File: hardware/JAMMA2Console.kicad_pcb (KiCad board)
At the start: 4 copper layers, 126 x 131.5 mm, 195 parts, among them J1 Conn_02x28_JAMMA, J10 Conn_02x03_Odd_Even, J11 Conn_02x05_Odd_Even, J12 Conn_01x03, J13 Conn_01x03, J2 DS1038-15FBNSiA74-0CC, J3 SCART-F, J4 DF1BZ-34DP-2.5DSA, J5 PJ-320D, J6 DS1037-15FNAKT74-0CC, J7 DS1037-15FNAKT74-0CC, J8 Phoenix PTS 1,5/4-5.0, J9 Molex 67503-1020, SW1 SW_Push, SW2 SW_Push, SW3 SW_Push, U1 USBLC6-2P6, U10 74LVC4245, U11 74LVC4245, U12 TL074, U13 LM1972, U14 TPA3138D2, U15 74HCT4053, U2 LD1117-3.3, U3 74HCT4053, U4 74HCT86, U5 74HCT4053, U6 LM1881, U7 THS7375, U8 STM32F103V8Tx, U9 74LVC4245, Y1 12MHz

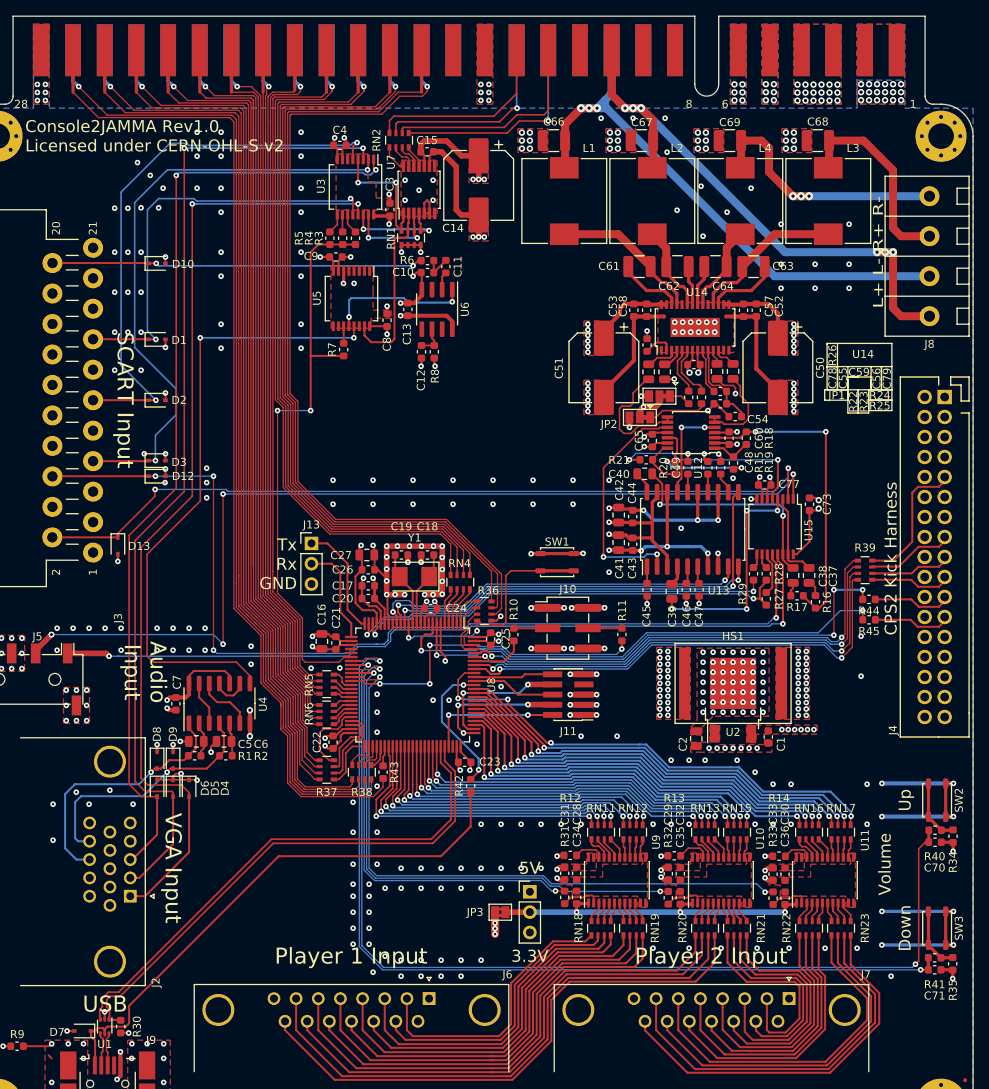
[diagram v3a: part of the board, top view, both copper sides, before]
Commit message: Started major rework on the Audio section (chose the wrong amplifier as it can't drive 4Ohm loads) Moved over to nightly Kicad v 5.9 versions. Was a mistake to do, but will look into reverting another time.
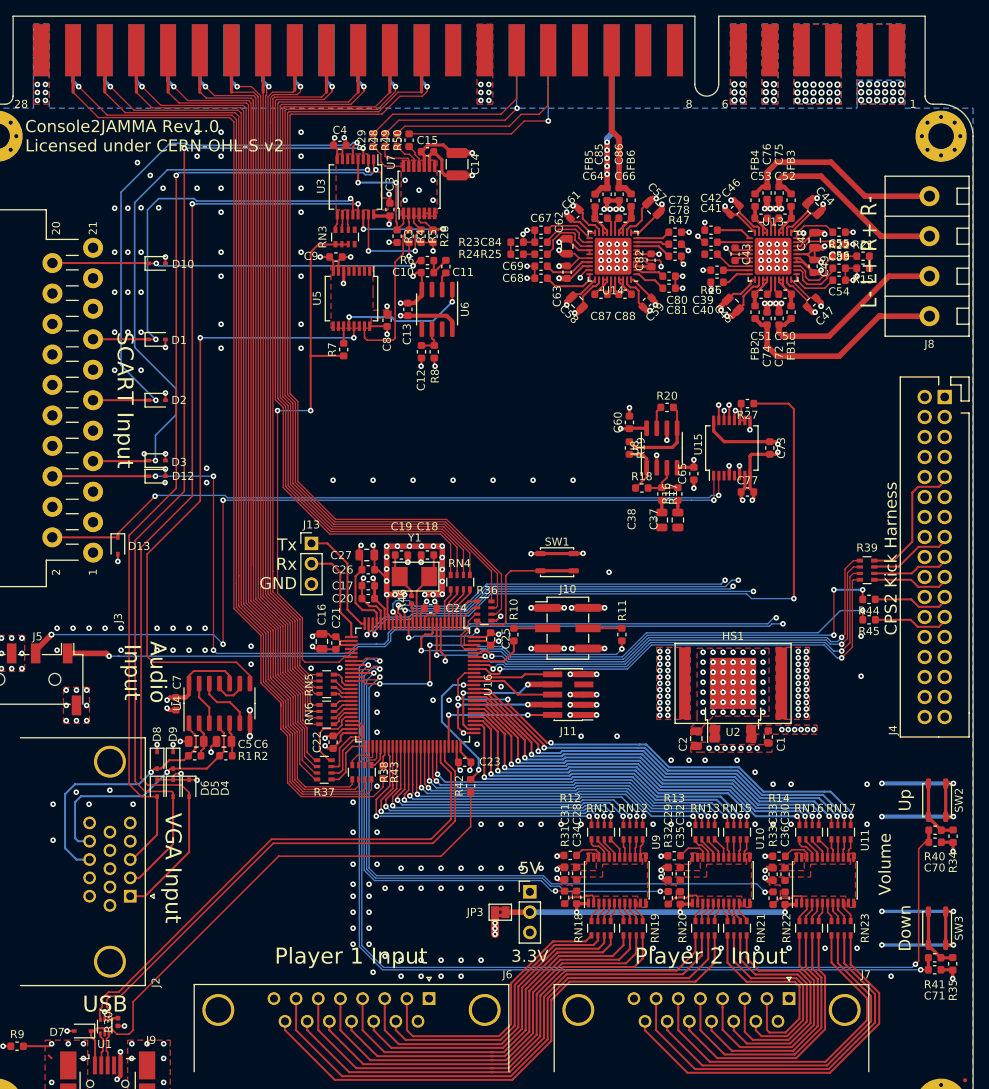
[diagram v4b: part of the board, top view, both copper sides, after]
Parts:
- removed JP1, JP2: SolderJumper_3_Bridged12, Jumper:SolderJumper-3_P1.3mm_Bridged12_Pad1.0x1.5mm
- removed L1, L2, L3, L4: 15u, Inductor_SMD:L_10.4x10.4_H4.8
- removed RN1, RN2: 75R, Resistor_SMD:R_Array_Convex_4x0603
- removed U12: TL074, Package_SO:TSSOP-14_4.4x5mm_P0.65mm
- added C72: 200p, Capacitor_SMD:C_0603_1608Metric, F.Cu at (137.8, 68.3)
- added C74: 200p, Capacitor_SMD:C_0603_1608Metric, F.Cu at (136.2, 68.3)
- added C75: 200p, Capacitor_SMD:C_0603_1608Metric, F.Cu at (137.8, 52.6)
- added C76: 200p, Capacitor_SMD:C_0603_1608Metric, F.Cu at (136.2, 52.6)
- added C80: 1u0, Capacitor_SMD:C_0603_1608Metric, F.Cu at (124.0, 63.0)
- added C81: 1u0, Capacitor_SMD:C_0603_1608Metric, F.Cu at (124.0, 64.5)
- added C82: 1u0, Capacitor_SMD:C_0603_1608Metric, F.Cu at (121.8, 61.0)
- added C83: 200p, Capacitor_SMD:C_0603_1608Metric, F.Cu at (145.2, 62.0)
- added C84: 200p, Capacitor_SMD:C_0603_1608Metric, F.Cu at (108.0, 58.8)
- added C85: 200p, Capacitor_SMD:C_0603_1608Metric, F.Cu at (116.2, 52.8)
- added C86: 200p, Capacitor_SMD:C_0603_1608Metric, F.Cu at (117.8, 52.8)
- added C87: 1u0, Capacitor_SMD:C_0603_1608Metric, F.Cu at (115.5, 65.2)
- added C88: 1u0, Capacitor_SMD:C_0603_1608Metric, F.Cu at (118.5, 65.2)
- added FB1: Ferrite_Bead_Small, Inductor_SMD:L_0603_1608Metric, F.Cu at (139.2, 67.5)
- added FB2: Ferrite_Bead_Small, Inductor_SMD:L_0603_1608Metric, F.Cu at (134.8, 67.5)
- added FB3: Ferrite_Bead_Small, Inductor_SMD:L_0603_1608Metric, F.Cu at (139.2, 53.5)
- added FB4: Ferrite_Bead_Small, Inductor_SMD:L_0603_1608Metric, F.Cu at (134.8, 53.5)
- added FB5: Ferrite_Bead_Small, Inductor_SMD:L_0603_1608Metric, F.Cu at (114.8, 53.5)
- added FB6: Ferrite_Bead_Small, Inductor_SMD:L_0603_1608Metric, F.Cu at (119.2, 53.5)
- added R46: 1K5, Resistor_SMD:R_0402_1005Metric, F.Cu at (91.8, 103.5)
- added R47: 10K, Resistor_SMD:R_0603_1608Metric, F.Cu at (124.8, 60.5)
- added R48: 75R, Resistor_SMD:R_0603_1608Metric, F.Cu at (88.5, 46.0)
- added R49: 75R, Resistor_SMD:R_0603_1608Metric, F.Cu at (90.0, 46.0)
- added R50: 75R, Resistor_SMD:R_0603_1608Metric, F.Cu at (91.5, 46.0)
- added RN3: 4K7, Resistor_SMD:R_Array_Convex_4x0603, F.Cu at (83.5, 58.1)
- added U16: STM32F103VCT6, Package_QFP:LQFP-100_14x14mm_P0.5mm, F.Cu at (92.0, 114.1)
- C14: footprint Capacitor_SMD:CP_Elec_8x10.5 -> Capacitor_SMD:C_1210_3225Metric
- C18, C19: value C_Small -> 8p
- C39, C40: footprint Capacitor_SMD:C_0805_2012Metric -> Capacitor_SMD:C_0603_1608Metric
- C41, C42, C55, C56, C78, C79: value 10u -> 1u0; footprint Capacitor_SMD:C_0805_2012Metric -> Capacitor_SMD:C_0603_1608Metric
- C43, C52, C53: value 100n -> 1u0
- C44: value 100n -> 10u; footprint Capacitor_SMD:C_0603_1608Metric -> Capacitor_SMD:C_0805_2012Metric
- C45, C48: value 1u0 -> 10u; footprint Capacitor_SMD:C_0603_1608Metric -> Capacitor_SMD:C_0805_2012Metric
- C49: value 1u0 -> 100n
- C50, C51: value 100u -> 1u0; footprint Capacitor_SMD:CP_Elec_8x10.5 -> Capacitor_SMD:C_0603_1608Metric
- C57, C58: value 10n -> 10u; footprint Capacitor_SMD:C_0603_1608Metric -> Capacitor_SMD:C_0805_2012Metric
- C61, C64: value 220n -> 1u0; footprint Capacitor_SMD:C_1210_3225Metric -> Capacitor_SMD:C_0603_1608Metric
- C62: value 220n -> 10u; footprint Capacitor_SMD:C_1210_3225Metric -> Capacitor_SMD:C_0805_2012Metric
- C63: value 220n -> 100n; footprint Capacitor_SMD:C_1210_3225Metric -> Capacitor_SMD:C_0603_1608Metric
- C66, C67, C68, C69: value 2u2 -> 1u0; footprint Capacitor_SMD:C_1210_3225Metric -> Capacitor_SMD:C_0603_1608Metric
- R15: value 2K -> 10K
- R16, R17, R19, R20, R26: value 100K -> 10K
- R18: value 47K -> 4K7
- R22: value 10K -> 100K
- R24: value R_Small -> 10K
- R25: value R_Small -> 100K
- R28, R29, R3, R4, R5: value 4K7 -> 75R
- R30: footprint Resistor_SMD:R_0603_1608Metric -> Resistor_SMD:R_0402_1005Metric
- R6: value 620 -> 620R
- U13: value LM1972 -> PAM8610; footprint Package_SO:SOIC-20W_7.5x12.8mm_P1.27mm -> Package_DFN_QFN:QFN-40-1EP_6x6mm_P0.5mm_EP4.6x4.6mm
- U14: value TPA3138D2 -> PAM8610; footprint Package_SO:TSSOP-28-1EP_4.4x9.7mm_P0.65mm -> Package_DFN_QFN:QFN-40-1EP_6x6mm_P0.5mm_EP4.6x4.6mm
- U8: value STM32F103V8Tx -> TL072; footprint Package_QFP:LQFP-100_14x14mm_P0.5mm -> Package_SO:SOIC-8_3.9x4.9mm_P1.27mm
- moved R29 72.1 mm to (87.0, 46.0)
- moved R28 59.3 mm to (94.5, 58.0), turned to -90 degrees
- moved C46 47.8 mm to (132.2, 54.8), turned to -135 degrees
- moved C44 44.7 mm to (142.0, 54.5), turned to -45 degrees
- moved U8 43.0 mm to (123.1, 84.5), turned to 90 degrees
- moved C39 40.5 mm to (130.0, 62.2), turned to 180 degrees
- moved C41 39.3 mm to (129.2, 58.8), turned to 180 degrees
- moved C68 38.6 mm to (108.0, 63.2), turned to 0 degrees
- moved C47 38.6 mm to (141.8, 66.2), turned to 45 degrees
- moved C43 38.4 mm to (132.2, 60.2), turned to -90 degrees
- moved C42 37.4 mm to (129.2, 57.2), turned to 180 degrees
- moved C45 37.2 mm to (132.0, 66.6), turned to 135 degrees
- moved R21 37.2 mm to (148.2, 60.5)
- moved U13 35.6 mm to (137.0, 60.5), turned to 0 degrees
- moved C48 31.4 mm to (142.2, 58.5)
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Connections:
- net /Audio/EXT_Audio_L renamed /EXT_Audio_L
- net /Audio/EXT_Audio_R renamed /EXT_Audio_R
- net /Digital I/O/P1_1 renamed /P1_1
- net /Digital I/O/P1_10 renamed /P1_10
- net /Digital I/O/P1_11 renamed /P1_11
- net /Digital I/O/P1_12 renamed /P1_12
- net /Digital I/O/P1_2 renamed /P1_2
- net /Digital I/O/P1_3 renamed /P1_3
- net /Digital I/O/P1_4 renamed /P1_4
- net /Digital I/O/P1_5 renamed /P1_5
- net /Digital I/O/P1_6 renamed /P1_6
- net /Digital I/O/P1_7 renamed /P1_7
- net /Digital I/O/P1_8 renamed /P1_8
- net /Digital I/O/P1_9 renamed /P1_9
- net /Digital I/O/P2_1 renamed /P2_1
- net /Digital I/O/P2_10 renamed /P2_10
- net /Digital I/O/P2_11 renamed /P2_11
- net /Digital I/O/P2_12 renamed /P2_12
- net /Digital I/O/P2_2 renamed /P2_2
- net /Digital I/O/P2_3 renamed /P2_3
- net /Digital I/O/P2_4 renamed /P2_4
- net /Digital I/O/P2_5 renamed /P2_5
- net /Digital I/O/P2_6 renamed /P2_6
- net /Digital I/O/P2_7 renamed /P2_7
- net /Digital I/O/P2_8 renamed /P2_8
- net /Digital I/O/P2_9 renamed /P2_9
- net /Digital I/O/VCC renamed /VCC
- C39 pad 2: /Audio/Audio_~Mono~_L -> /Audio/Audio_L
- C40 pad 2: /Audio/Audio_R -> GND
- C41 pad 1: -5V -> Net-(C41-Pad1)
- C41 pad 2: GND -> /Audio/Audio_R
- C42 pad 1: +5V -> Net-(C42-Pad1)
- C43 pad 1: -5V -> Net-(C43-Pad1)
- C44 pad 1: +5V -> +12V
- C45 pad 1: Net-(C45-Pad1) -> +12V
- C46 pad 1: Net-(C46-Pad1) -> +12V
- C47 pad 1: Net-(C47-Pad1) -> +12V
- C48 pad 1: Net-(C48-Pad1) -> +12V
- C49 pad 1: Net-(C49-Pad1) -> +12V
- C50 pad 1: +12V -> Net-(C50-Pad1)
- C50 pad 2: GND -> Net-(C50-Pad2)
- C51 pad 1: +12V -> Net-(C51-Pad1)
- C51 pad 2: GND -> Net-(C51-Pad2)
- C52 pad 1: +12V -> Net-(C52-Pad1)
- C52 pad 2: GND -> Net-(C52-Pad2)
- C53 pad 1: +12V -> Net-(C53-Pad1)
- C53 pad 2: GND -> Net-(C53-Pad2)
- C54 pad 1: Net-(C54-Pad1) -> GND
- C54 pad 2: GND -> Net-(C54-Pad2)
- C55 pad 1: Net-(C55-Pad1) -> GND
- C55 pad 2: GND -> Net-(C55-Pad2)
- C56 pad 1: Net-(C56-Pad1) -> GND
- C56 pad 2: GND -> Net-(C56-Pad2)
- C61 pad 1: Net-(C61-Pad1) -> +12V
- C61 pad 2: Net-(C61-Pad2) -> GND
- C62 pad 1: Net-(C62-Pad1) -> +12V
- C62 pad 2: Net-(C62-Pad2) -> GND
- C63 pad 1: Net-(C63-Pad1) -> +12V
- C63 pad 2: Net-(C63-Pad2) -> GND
- C66 pad 1: /Speaker_JAMMA- -> Net-(C66-Pad1)
- C66 pad 2: GND -> Net-(C66-Pad2)
- C67 pad 2: /Speaker_JAMMA+ -> Net-(C67-Pad2)
- C68 pad 1: /Audio/Speaker_R+ -> GND
- C68 pad 2: GND -> Net-(C68-Pad2)
- C69 pad 2: /Audio/Speaker_R- -> Net-(C69-Pad2)
- C78 pad 2: Net-(C78-Pad2) -> /Audio/Audio_Mono
- C79 pad 2: Net-(C79-Pad2) -> GND
- J1 pad 11: Net-(J1-Pad11) -> (no net)
- J1 pad 15: Net-(J1-Pad15) -> (no net)
- J1 pad 8: Net-(J1-Pad8) -> (no net)
- J1 pad 9: Net-(J1-Pad9) -> (no net)
- J1 pad J: Net-(J1-PadJ) -> (no net)
- J1 pad K: Net-(J1-PadK) -> (no net)
- J1 pad M: Net-(J1-PadM) -> (no net)
- J1 pad R: Net-(J1-PadR) -> (no net)
- J1 pad S: Net-(J1-PadS) -> (no net)
- J11 pad 7: Net-(J11-Pad7) -> (no net)
- J13 pad 1: /Digital I/O/UART_TX -> /UART_TX
- J13 pad 2: /Digital I/O/UART_RX -> /UART_RX
- J2 pad 11: Net-(J2-Pad11) -> (no net)
- J2 pad 12: Net-(J2-Pad12) -> (no net)
- J2 pad 15: Net-(J2-Pad15) -> (no net)
- J2 pad 4: Net-(J2-Pad4) -> (no net)
- J2 pad 9: Net-(J2-Pad9) -> (no net)
- J3 pad 1: Net-(J3-Pad1) -> (no net)
- J3 pad 10: Net-(J3-Pad10) -> (no net)
- J3 pad 12: Net-(J3-Pad12) -> (no net)
- J3 pad 16: Net-(J3-Pad16) -> (no net)
- J3 pad 19: Net-(J3-Pad19) -> (no net)
- J3 pad 3: Net-(J3-Pad3) -> (no net)
- J3 pad 8: Net-(J3-Pad8) -> (no net)
- J4 pad 1: Net-(J4-Pad1) -> (no net)
- J4 pad 10: Net-(J4-Pad10) -> (no net)
- J4 pad 11: Net-(J4-Pad11) -> (no net)
- J4 pad 12: Net-(J4-Pad12) -> (no net)
- J4 pad 13: Net-(J4-Pad13) -> (no net)
- J4 pad 14: Net-(J4-Pad14) -> (no net)
- J4 pad 16: Net-(J4-Pad16) -> (no net)
- J4 pad 18: Net-(J4-Pad18) -> (no net)
- J4 pad 2: Net-(J4-Pad2) -> (no net)
- J4 pad 20: Net-(J4-Pad20) -> (no net)
- J4 pad 22: Net-(J4-Pad22) -> (no net)
- J4 pad 24: Net-(J4-Pad24) -> (no net)
- J4 pad 25: Net-(J4-Pad25) -> (no net)
- J4 pad 26: Net-(J4-Pad26) -> (no net)
- J4 pad 27: Net-(J4-Pad27) -> (no net)
- J4 pad 28: Net-(J4-Pad28) -> (no net)
- J4 pad 29: Net-(J4-Pad29) -> (no net)
- J4 pad 3: Net-(J4-Pad3) -> (no net)
- J4 pad 30: Net-(J4-Pad30) -> (no net)
- J4 pad 32: Net-(J4-Pad32) -> (no net)
- J4 pad 4: Net-(J4-Pad4) -> (no net)
- J4 pad 5: Net-(J4-Pad5) -> (no net)
- J4 pad 6: Net-(J4-Pad6) -> (no net)
- J4 pad 7: Net-(J4-Pad7) -> (no net)
- J4 pad 8: Net-(J4-Pad8) -> (no net)
- J6 pad 9: Net-(J6-Pad9) -> (no net)
- J7 pad 9: Net-(J7-Pad9) -> (no net)
- J8 pad 1: /Speaker_JAMMA+ -> /Speaker_L-
- J8 pad 2: /Speaker_JAMMA- -> /Speaker_L+
- J8 pad 3: /Audio/Speaker_R+ -> /Speaker_R+
- J8 pad 4: /Audio/Speaker_R- -> /Speaker_R-
- J9 pad 4: Net-(J9-Pad4) -> (no net)
- R20 pad 1: Net-(R20-Pad1) -> /Audio/Audio_Mono
- R21 pad 1: /Audio/Audio_Mono -> Net-(R21-Pad1)
- R21 pad 2: Net-(R20-Pad1) -> Net-(R15-Pad1)
- R22 pad 2: Net-(JP1-Pad1) -> Net-(R21-Pad1)
- R23 pad 2: Net-(JP2-Pad1) -> GND
- R24 pad 2: Net-(C54-Pad1) -> Net-(R23-Pad1)
- R25 pad 1: Net-(C54-Pad1) -> Net-(R25-Pad1)
- R25 pad 2: GND -> Net-(R24-Pad1)
- R26 pad 1: +12V -> Net-(R26-Pad1)
- R26 pad 2: Net-(R26-Pad2) -> +3V3
- R28 pad 1: /Audio_Select_~SCART~_EXT -> /Video/Video_Green
- R28 pad 2: Net-(R28-Pad2) -> GND
- R29 pad 1: /Audio_Select_~Mono~_Stereo -> Net-(R29-Pad1)
- R29 pad 2: Net-(R29-Pad2) -> /Video_Blue
- R3 pad 1: /Video_Select_~SCART~_VGA -> /Video/Video_Blue
- R3 pad 2: Net-(R3-Pad2) -> GND
- R30 pad 2: /Digital I/O/USB_D+ -> /USB_D+
- R4 pad 1: /Video_Select_~SCART~_VGA -> /Video/Video_CSYNC
- R4 pad 2: Net-(R4-Pad2) -> GND
- R42 pad 2: /Digital I/O/USB_Detect -> /USB_Detect
- R5 pad 1: /Video_Select_~SCART~_VGA -> /Video/Video_Red
- R5 pad 2: Net-(R5-Pad2) -> GND
- U1 pad 1: /Digital I/O/USB_D+ -> /USB_D+
- U1 pad 3: /Digital I/O/USB_D- -> /USB_D-
- U13 pad 1: Net-(C45-Pad1) -> Net-(C42-Pad1)
- U13 pad 10: /VOL_LOAD_SHIFT -> Net-(C40-Pad1)
- U13 pad 11: /VOL_DATA_IN -> GND
- U13 pad 12: Net-(R15-Pad1) -> +12V
- U13 pad 13: +5V -> Net-(C51-Pad2)
- U13 pad 14: Net-(C48-Pad1) -> Net-(C51-Pad2)
- U13 pad 15: +5V -> Net-(C51-Pad1)
- U13 pad 16: Net-(C49-Pad1) -> Net-(C50-Pad2)
- U13 pad 17: Net-(U12-Pad5) -> Net-(C50-Pad1)
- U13 pad 18: -5V -> Net-(C50-Pad1)
- U13 pad 19: GND -> +12V
- U13 pad 2: Net-(U12-Pad10) -> Net-(C41-Pad1)
- U13 pad 20: Net-(C40-Pad1) -> GND
- U13 pad 3: GND -> Net-(C43-Pad1)
- U13 pad 4: Net-(C39-Pad1) -> Net-(C43-Pad1)
- U13 pad 5: Net-(C46-Pad1) -> /Volume
- U13 pad 6: Net-(C47-Pad1) -> GND
- U13 pad 7: -5V -> GND
- U13 pad 8: GND -> Net-(R26-Pad1)
- U13 pad 9: /VOL_CLK -> Net-(C39-Pad1)
- U14 pad 10: Net-(C54-Pad1) -> Net-(C79-Pad1)
- U14 pad 11: Net-(C56-Pad1) -> GND
- U14 pad 12: Net-(C79-Pad1) -> +12V
- U14 pad 13: Net-(U14-Pad13) -> Net-(C66-Pad2)
- U14 pad 14: GND -> Net-(C66-Pad2)
- U14 pad 15: +12V -> Net-(C66-Pad1)
- U14 pad 16: +12V -> Net-(C64-Pad2)
- U14 pad 17: Net-(C63-Pad1) -> Net-(C64-Pad1)
- U14 pad 18: Net-(C63-Pad2) -> Net-(C64-Pad1)
- U14 pad 19: GND -> +12V
- U14 pad 2: Net-(R26-Pad2) -> Net-(C80-Pad1)
- U14 pad 20: Net-(C64-Pad1) -> GND
- U14 pad 21: Net-(C64-Pad2) -> Net-(C67-Pad2)
- U14 pad 22: Net-(C62-Pad2) -> Net-(C84-Pad1)
- U14 pad 23: Net-(C62-Pad1) -> Net-(R25-Pad1)
- U14 pad 25: Net-(C61-Pad2) -> GND
- U14 pad 26: Net-(C61-Pad1) -> +12V
- U14 pad 27: +12V -> Net-(C69-Pad2)
- U14 pad 28: +12V -> GND
- U14 pad 29: GND -> (no net)
- U14 pad 3: Net-(C78-Pad1) -> Net-(C82-Pad1)
- U14 pad 4: Net-(C55-Pad1) -> Net-(C82-Pad1)
- U14 pad 5: Net-(R22-Pad1) -> /Volume
- U14 pad 6: Net-(R23-Pad1) -> GND
- U14 pad 7: +12V -> GND
- U14 pad 8: GND -> Net-(R47-Pad1)
- U14 pad 9: Net-(R24-Pad1) -> Net-(C78-Pad1)
- U15 pad 10: Net-(R28-Pad2) -> Net-(R27-Pad2)
- U15 pad 3: /Audio/Audio_L -> (no net)
- U15 pad 4: /Audio/Audio_~Mono~_L -> GND
- U15 pad 5: /Audio/Audio_Mono -> (no net)
- U15 pad 9: Net-(R29-Pad2) -> GND
- U3 pad 10: Net-(R4-Pad2) -> Net-(RN3-Pad7)
- U3 pad 11: Net-(R3-Pad2) -> Net-(RN3-Pad6)
- U3 pad 9: Net-(R5-Pad2) -> Net-(RN3-Pad8)
- U5 pad 1: Net-(U5-Pad1) -> (no net)
- U5 pad 2: Net-(U5-Pad2) -> (no net)
- U5 pad 3: Net-(U5-Pad3) -> (no net)
- U5 pad 5: Net-(U5-Pad5) -> (no net)
- U6 pad 3: Net-(U6-Pad3) -> (no net)
- U6 pad 5: Net-(U6-Pad5) -> (no net)
- U6 pad 7: Net-(U6-Pad7) -> (no net)
- U7 pad 14: Net-(RN2-Pad1) -> Net-(R29-Pad1)
- U7 pad 7: Net-(U7-Pad7) -> (no net)
- U7 pad 8: Net-(U7-Pad8) -> (no net)
- U8 pad 1: Net-(R36-Pad5) -> Net-(R18-Pad1)
- U8 pad 2: Net-(RN4-Pad8) -> GND
- U8 pad 3: Net-(RN4-Pad7) -> Net-(R16-Pad1)
- U8 pad 4: Net-(RN4-Pad6) -> -5V
- U8 pad 5: Net-(RN4-Pad5) -> Net-(R19-Pad1)
- U8 pad 6: +3V3 -> GND
- U8 pad 7: Net-(R44-Pad2) -> /Audio/Audio_Mono
- U8 pad 8: Net-(R45-Pad2) -> +5V
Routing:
- net /Digital I/O/USB_D+: track 66.7 -> 0.00 mm
- net /USB_D+: track 0.00 -> 66.6 mm
- net /USB_D-: track 0.00 -> 65.4 mm
- net /Digital I/O/USB_D-: track 65.4 -> 0.00 mm
- net /VOL_DATA_IN: track 56.0 -> 0.00 mm, vias 2 -> 0
- net /Speaker_JAMMA+: track 73.4 -> 19.4 mm, vias 6 -> 0
- net /Speaker_JAMMA-: track 74.0 -> 23.3 mm, vias 3 -> 5
- net /VOL_LOAD_SHIFT: track 48.3 -> 0.00 mm, vias 2 -> 0
- net /VOL_CLK: track 47.8 -> 0.00 mm, vias 2 -> 0
- net Net-(U16-Pad16): track 0.00 -> 46.6 mm, vias 0 -> 2
- net Net-(U16-Pad17): track 0.00 -> 46.0 mm, vias 0 -> 2
- net Net-(U16-Pad15): track 0.00 -> 44.0 mm, vias 0 -> 2
- net /Audio/Speaker_R-: track 33.6 -> 0.00 mm, vias 3 -> 0
- net Net-(R16-Pad1): track 39.2 -> 6.48 mm, vias 2 -> 0
- net Net-(U12-Pad10): track 29.6 -> 0.00 mm, vias 2 -> 0
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- added copper zone on F.Cu, net Net-(C82-Pad1)
- removed copper zone on In2.Cu, net +12V
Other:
- rule via_min_size: 0.7 -> 0.6
- board text added: "L- L+ R+ R-"
- board text removed: "L+ L- R+ R-"
- board text removed: "U14"

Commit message: Pushing work I did a few months ago and I forgot to push. Identified some mistakes which I'll fix in a future commit.
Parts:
- removed R24: 10K, Resistor_SMD:R_0603_1608Metric
- removed R25: 100K, Resistor_SMD:R_0603_1608Metric
- removed U14: PAM8610, Package_DFN_QFN:QFN-40-1EP_6x6mm_P0.5mm_EP4.6x4.6mm
- added R51: 10K, Resistor_SMD:R_0603_1608Metric, F.Cu at (125.5, 87.6)
- added U12: PAM8610, Console2JAMMA:QFN-40-1EP_6x6mm_P0.5mm_EP4.6x4.6mm_ThermalVias, F.Cu at (137.0, 60.5)
- C83, C84: value 200p -> 10n
- JP3: footprint Jumper:SolderJumper-2_P1.3mm_Bridged2Bar_Pad1.0x1.5mm -> Jumper:SolderJumper-2_P1.3mm_Open_TrianglePad1.0x1.5mm
- R15, R21, R23: value 10K -> 4K7
- R18: value 4K7 -> 10K
- R22: value 100K -> 4K7
- R30, R46: footprint Resistor_SMD:R_0402_1005Metric -> Resistor_SMD:R_0603_1608Metric
- U13: footprint Package_DFN_QFN:QFN-40-1EP_6x6mm_P0.5mm_EP4.6x4.6mm -> Console2JAMMA:QFN-40-1EP_6x6mm_P0.5mm_EP4.6x4.6mm_ThermalVias
- moved R21 42.5 mm to (105.8, 59.5), turned to 90 degrees
- moved U13 20.0 mm to (117.0, 60.5), turned to 180 degrees
- moved C37 11.1 mm to (129.5, 83.2), turned to 0 degrees
- moved C38 10.4 mm to (129.5, 85.2), turned to 0 degrees
- moved R20 9.83 mm to (115.4, 84.6), turned to 90 degrees
- moved C60 8.22 mm to (117.3, 89.3), turned to 180 degrees
- moved C65 7.28 mm to (123.7, 81.2), turned to 180 degrees
- moved R16 7.06 mm to (126.2, 83.2), turned to 0 degrees
- moved R18 6.63 mm to (127.0, 87.6), turned to 90 degrees
- moved R17 5.87 mm to (126.2, 85.2), turned to 0 degrees
- moved R19 5.03 mm to (120.5, 89.3), turned to 0 degrees
- moved R27 4.08 mm to (137.2, 81.2)
- moved C73 4.02 mm to (139.9, 86.7)
- moved C77 4.02 mm to (137.1, 92.2)
- moved U15 4.02 mm to (135.2, 86.7)
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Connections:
- net /UART_RX renamed /Digital I/O/UART_Rx
- net /UART_TX renamed /Digital I/O/UART_Tx
- C37 pad 2: /Audio/Audio_L -> /Audio/Audio_R
- C38 pad 2: /Audio/Audio_R -> /Audio/Audio_L
- JP3 pad 1: /VCC -> Net-(J6-Pad1)
- JP3 pad 2: Net-(J6-Pad1) -> /VCC
- R21 pad 2: Net-(R15-Pad1) -> GND
- R22 pad 1: Net-(R22-Pad1) -> Net-(R15-Pad1)
- R22 pad 2: Net-(R21-Pad1) -> GND
- R23 pad 1: Net-(R23-Pad1) -> Net-(R21-Pad1)
- R26 pad 2: +3V3 -> +5V
- R47 pad 2: +3V3 -> +5V
- RN20 pad 1: /P1_9 -> /P2_8
- RN20 pad 2: /P1_10 -> /P2_7
- RN20 pad 3: /P1_11 -> /P2_6
- RN20 pad 4: /P1_12 -> /P2_5
- RN21 pad 1: /P2_1 -> /P2_4
- RN21 pad 2: /P2_2 -> /P2_3
- RN21 pad 3: /P2_3 -> /P2_2
- RN21 pad 4: /P2_4 -> /P2_1
- RN22 pad 1: /P2_5 -> /P2_9
- RN22 pad 2: /P2_6 -> /P2_10
- RN22 pad 3: /P2_7 -> /P2_11
- RN22 pad 4: /P2_8 -> /P2_12
- RN23 pad 1: /P2_9 -> /P1_9
- RN23 pad 2: /P2_10 -> /P1_10
- RN23 pad 3: /P2_11 -> /P1_11
- RN23 pad 4: /P2_12 -> /P1_12
- U13 pad 1: Net-(C42-Pad1) -> Net-(C81-Pad1)
- U13 pad 10: Net-(C40-Pad1) -> Net-(C79-Pad1)
- U13 pad 13: Net-(C51-Pad2) -> Net-(C66-Pad2)
- U13 pad 14: Net-(C51-Pad2) -> Net-(C66-Pad2)
- U13 pad 15: Net-(C51-Pad1) -> Net-(C66-Pad1)
- U13 pad 16: Net-(C50-Pad2) -> Net-(C64-Pad2)
- U13 pad 17: Net-(C50-Pad1) -> Net-(C64-Pad1)
- U13 pad 18: Net-(C50-Pad1) -> Net-(C64-Pad1)
- U13 pad 2: Net-(C41-Pad1) -> Net-(C80-Pad1)
- U13 pad 21: Net-(C54-Pad2) -> Net-(C67-Pad2)
- U13 pad 22: Net-(C83-Pad1) -> Net-(C84-Pad1)
- U13 pad 23: Net-(R22-Pad1) -> Net-(R21-Pad1)
- U13 pad 27: Net-(C56-Pad2) -> Net-(C69-Pad2)
- U13 pad 29: (no net) -> /~Mono_Shutdown~
- U13 pad 3: Net-(C43-Pad1) -> Net-(C82-Pad1)
- U13 pad 30: Net-(C55-Pad2) -> Net-(C68-Pad2)
- U13 pad 33: Net-(C52-Pad1) -> Net-(C87-Pad1)
- U13 pad 34: Net-(C52-Pad1) -> Net-(C87-Pad1)
- U13 pad 35: Net-(C52-Pad2) -> Net-(C87-Pad2)
- U13 pad 36: Net-(C53-Pad1) -> Net-(C88-Pad1)
- U13 pad 37: Net-(C53-Pad2) -> Net-(C88-Pad2)
- U13 pad 38: Net-(C53-Pad2) -> Net-(C88-Pad2)
- U13 pad 4: Net-(C43-Pad1) -> Net-(C82-Pad1)
- U13 pad 41: (no net) -> Net-(U13-Pad41)
- U13 pad 8: Net-(R26-Pad1) -> Net-(R47-Pad1)
- U13 pad 9: Net-(C39-Pad1) -> Net-(C78-Pad1)
- U15 pad 12: /SCART_Audio_L -> (no net)
- U15 pad 13: /EXT_Audio_L -> (no net)
- U15 pad 15: /Audio/Audio_L -> GND
- U15 pad 3: (no net) -> /EXT_Audio_L
- U15 pad 4: GND -> /Audio/Audio_L
- U15 pad 5: (no net) -> /SCART_Audio_L
- U16 pad 15: (no net) -> /~Mono_Shutdown~
- U16 pad 24: (no net) -> /~Stereo_Shutdown~
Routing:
- net /Volume: track 7.10 -> 118.2 mm
- net /~Stereo_Shutdown~: track 0.00 -> 104.9 mm, vias 0 -> 2
- net /~Mono_Shutdown~: track 0.00 -> 68.5 mm, vias 0 -> 4
- net /Audio_Select_~Mono~_Stereo: track 52.0 -> 0.00 mm, vias 2 -> 0
- net Net-(U16-Pad16): track 46.6 -> 0.00 mm, vias 2 -> 0
- net Net-(U16-Pad17): track 46.0 -> 0.00 mm, vias 2 -> 0
- net Net-(U16-Pad15): track 44.0 -> 0.00 mm, vias 2 -> 0
- net +5V: track 148.4 -> 186.2 mm, vias 31 -> 36
- net /Audio/Audio_Mono: track 4.00 -> 37.4 mm, vias 1 -> 2
- net /Audio/Audio_R: track 2.41 -> 34.7 mm
- net /Audio/Audio_L: track 2.90 -> 33.2 mm
- net /P1_9: track 64.4 -> 90.4 mm
- net /P2_7: track 33.7 -> 7.97 mm
- net /P1_10: track 64.4 -> 90.1 mm
- net /P1_11: track 69.9 -> 95.3 mm
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- added copper zone on In2.Cu, net +12V
- added copper zone on F.Cu, net /VCC
- added copper zone on F.Cu, net Net-(C50-Pad1)
- added copper zone on F.Cu, net Net-(C51-Pad2)
- added copper zone on F.Cu, net Net-(C52-Pad1)
- added copper zone on F.Cu, net Net-(C53-Pad2)
- added copper zone on F.Cu, net Net-(C64-Pad1)
- added copper zone on F.Cu, net Net-(C66-Pad2)
- added copper zone on F.Cu, net Net-(C87-Pad1)
- added copper zone on F.Cu, net Net-(C88-Pad2)
- added copper zone on In2.Cu, net Net-(J9-Pad6)
- added copper zone on B.Cu, net Net-(U12-Pad41)
- added copper zone on In2.Cu, net Net-(U12-Pad41)
- added copper zone on B.Cu, net Net-(U13-Pad41)
- added copper zone on In2.Cu, net Net-(U13-Pad41)
- removed copper zone on F.Cu, net Net-(C82-Pad1)
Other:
- rule trace_min: 0.1524 -> 0.152
- board text added: "+12V"
- board text added: "+5V"
- board text added: "-5V"
- board text added: "Console2JAMMA Rev1.1 Licensed under CERN-OHL-S v2 Alexander Knapik"
- board text added: "GND"
- board text added: "L+"
- board text added: "L-"
- board text added: "R+"
- board text added: "R-"
- board text removed: "Console2JAMMA Rev1.0 Licensed under CERN-OHL-S v2"
- board text removed: "L- L+ R+ R-"

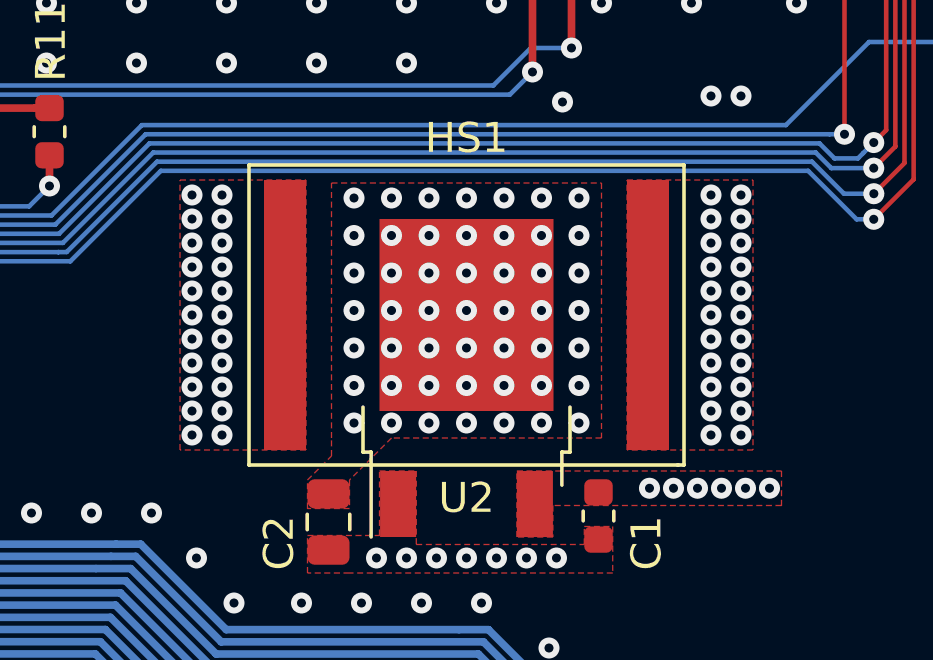
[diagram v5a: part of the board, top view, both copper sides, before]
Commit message: Updated the schematic & layout to fix the heat sink net issues with the 3v3 regulator.
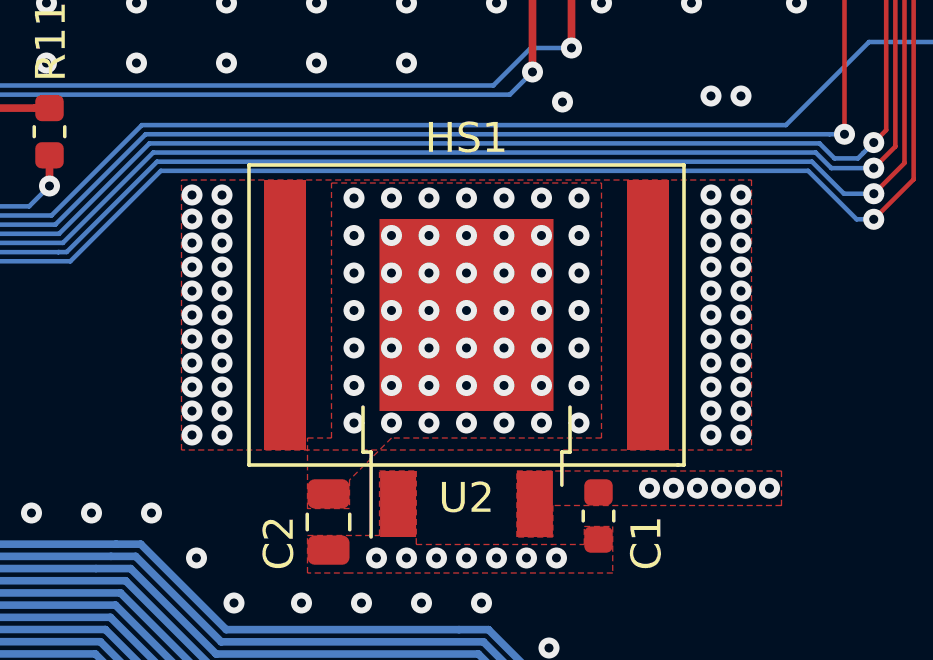
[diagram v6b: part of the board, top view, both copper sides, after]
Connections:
- HS1 pad 1: GND -> +3V3
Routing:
- net GND: vias 490 -> 446
- net +3V3: vias 76 -> 120
